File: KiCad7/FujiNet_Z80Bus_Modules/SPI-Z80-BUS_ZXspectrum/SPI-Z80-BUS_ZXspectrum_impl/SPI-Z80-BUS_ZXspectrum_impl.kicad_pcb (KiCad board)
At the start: 2 copper layers, 155 x 55 mm, 29 parts, among them IC1 74HC32N, J1 PinHeader_2.54mm, J2 Z80_CONTROL

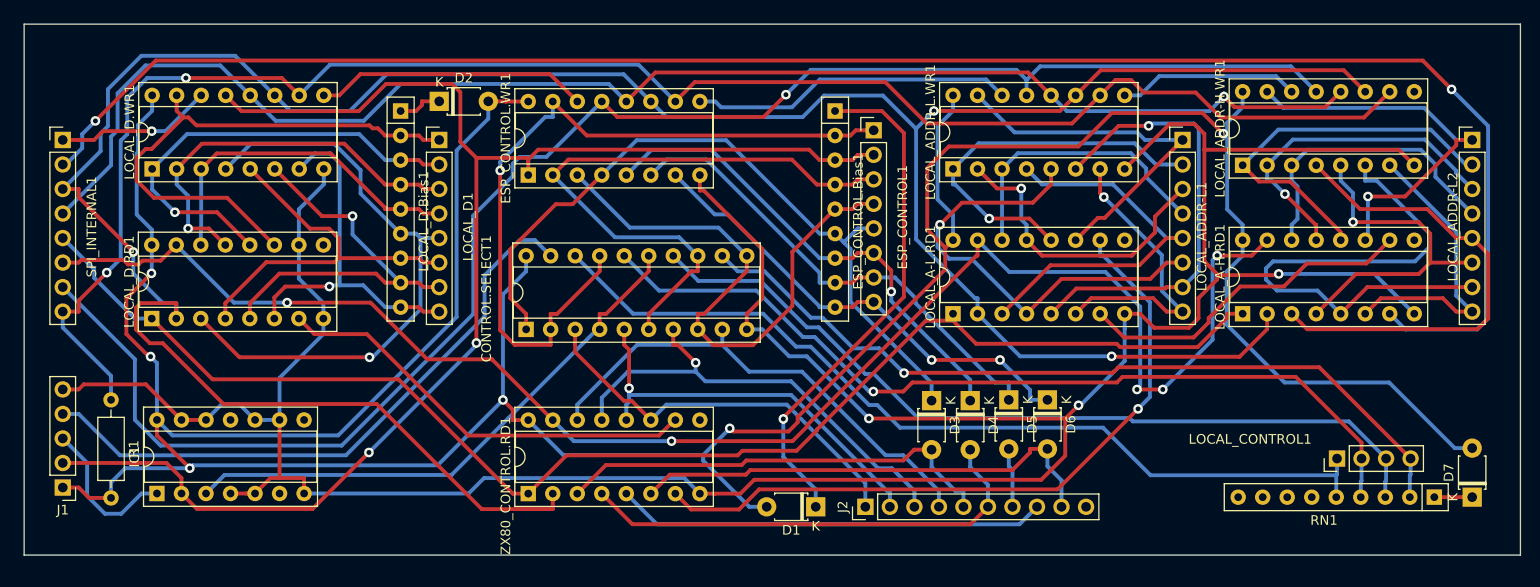
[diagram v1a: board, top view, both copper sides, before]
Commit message: KICad fixed SPI impl
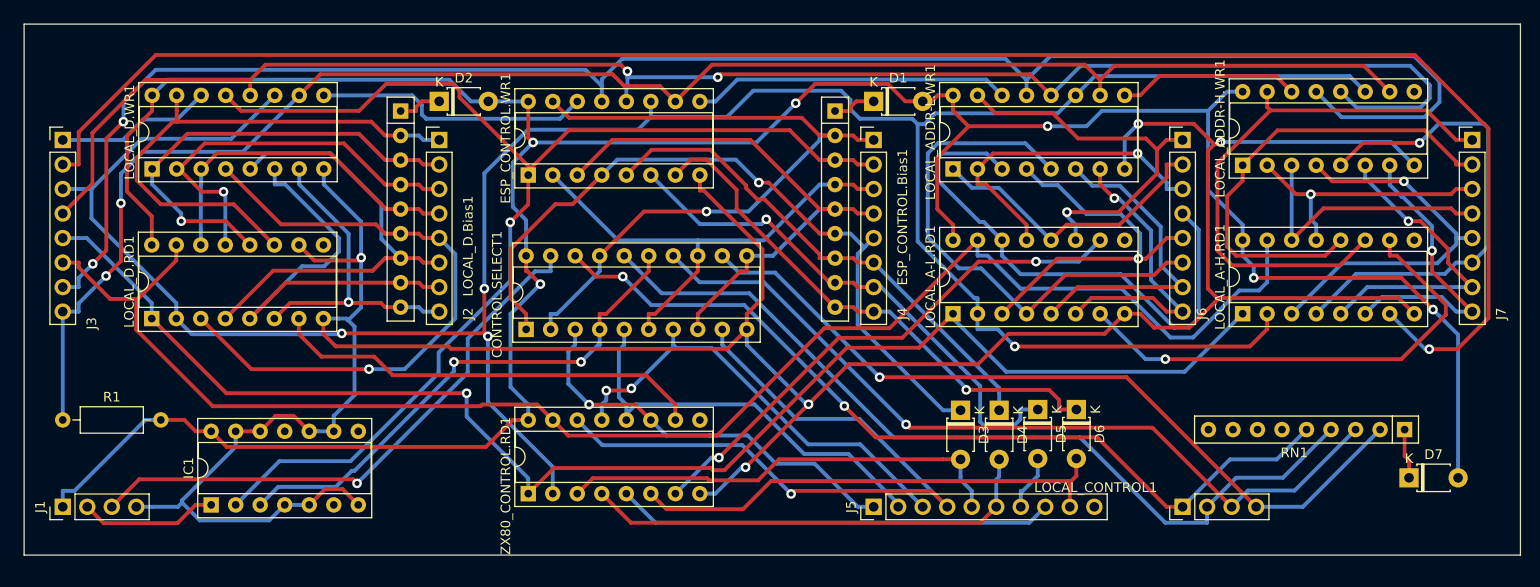
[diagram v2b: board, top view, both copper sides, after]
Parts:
- J1: footprint Connector_PinHeader_2.54mm:PinHeader_1x05_P2.54mm_Vertical -> Connector_PinHeader_2.54mm:PinHeader_1x04_P2.54mm_Vertical
- J2: renamed from LOCAL_D1; value PinHeader_2.54mm -> LOCAL_D
- J3: renamed from SPI_INTERNAL1; value PinHeader_2.54mm -> ESP_SPI_INT
- J4: renamed from ESP_CONTROL1; value PinHeader_2.54mm -> ESP_CONTROL
- J6: renamed from LOCAL_ADDR-L1; value PinHeader_2.54mm -> LOCAL_A-L
- J7: renamed from LOCAL_ADDR-L2; value PinHeader_2.54mm -> LOCAL_A-H
- LOCAL_CONTROL1: value PinHeader_2.54mm -> LOCAL_CONTROL
- moved D1 42.4 mm to (143.0, 35.0), turned to 0 degrees
- moved LOCAL_CONTROL1 16.8 mm to (175.0, 77.0)
- moved RN1 7.65 mm to (198.0, 69.0)
- moved D7 6.84 mm to (198.5, 74.0), turned to 0 degrees
- moved IC1 5.74 mm to (74.4, 76.8)
- moved R1 5.42 mm to (59.0, 68.0), turned to 0 degrees
- moved D3 3.16 mm to (152.0, 67.0)
- moved D4 3.16 mm to (156.0, 67.0)
- moved D5 3.16 mm to (160.0, 66.9)
- moved D6 3.16 mm to (164.0, 66.9)
- moved J1 2.00 mm to (59.0, 77.0), turned to 90 degrees
- moved J4 1.00 mm to (143.0, 39.0)
- moved J5 0.86 mm to (143.0, 77.0)
- renumbered J2 to J5
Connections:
- J1 pad 2: /SPI-Z80-BUS/ESP_CONTROL.WR -> /SPI-Z80-BUS/ESP_PULSE
- J1 pad 3: /SPI-Z80-BUS/ESP_PULSE -> /SPI-Z80-BUS/!ESP_HARDLOCK
- J1 pad 4: /SPI-Z80-BUS/!ESP_HARDLOCK -> GND
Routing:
- net +5V: track 362.0 -> 303.1 mm
- net Net-(D1-K): track 53.4 -> 4.65 mm, vias 1 -> 0
- net /SPI-Z80-BUS/LOCAL_A3: track 29.9 -> 56.1 mm
- net /SPI-Z80-BUS/Z80_CONTROL.MEMRQ: track 51.1 -> 74.2 mm, vias 0 -> 1
- net /SPI-Z80-BUS/ESP_SPI_INT.SCK: track 292.8 -> 270.0 mm, vias 3 -> 4
- net /SPI-Z80-BUS/ESP_CONTROL.WR: track 150.1 -> 127.9 mm, vias 2 -> 1
- net /SPI-Z80-BUS/LOCAL_A14: track 54.9 -> 32.9 mm, vias 0 -> 1
- net /SPI-Z80-BUS/ESP_SPI_INT.STC: track 152.1 -> 170.9 mm, vias 1 -> 2
- net Net-(LOCAL_A-L.RD1-DS): track 73.2 -> 54.9 mm, vias 1 -> 2
- net /SPI-Z80-BUS/ESP_SPI_INT.OE: track 168.2 -> 185.6 mm, vias 1 -> 2
- net /SPI-Z80-BUS/LOCAL_A8: track 41.5 -> 58.1 mm, vias 1 -> 0
- net Net-(LOCAL_A-H.RD1-DS): track 35.5 -> 50.2 mm, vias 0 -> 1
- net /SPI-Z80-BUS/LOCAL_A13: track 36.3 -> 50.2 mm
- net /SPI-Z80-BUS/LOCAL_A6: track 46.8 -> 33.3 mm, vias 1 -> 0
- net /SPI-Z80-BUS/ESP_CONTROL.IORQ: track 63.8 -> 50.3 mm
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
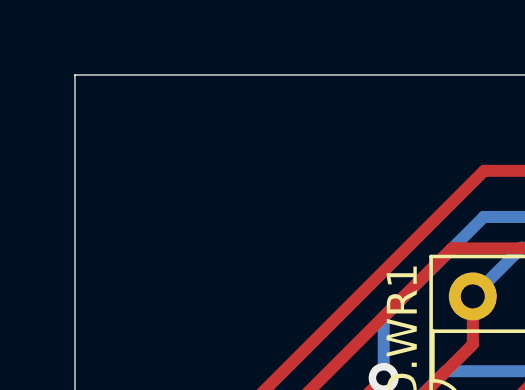
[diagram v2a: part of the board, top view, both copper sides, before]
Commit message: KiCad Corrected the orientation of the impl PCBs
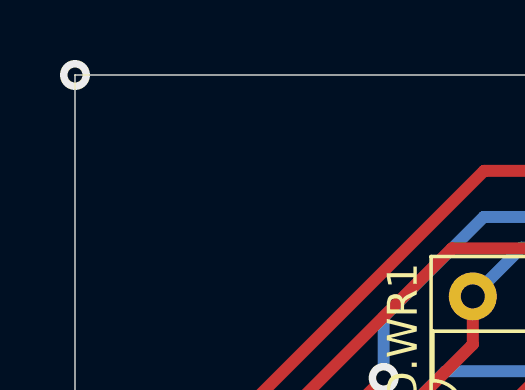
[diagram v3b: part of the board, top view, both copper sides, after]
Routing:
- net (no net): vias 0 -> 1
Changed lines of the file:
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@@
     (style (thickness 0.1) (arrow_length 1.27) (text_position_mode 0) (extension_height 0.58642) (extension_offset 0.5) keep_text_aligned)
   )
+  (via (at 55 27) (size 1) (drill 0.5) (layers "F.Cu" "B.Cu") (net 0))
   (segment (start 138.5079 48.7) (end 139 48.7) (width 0.4) (layer "F.Cu") (net 1))
   (segment (start 132.1147 43.4148) (end 137.3999 48.7) (width 0.4) (layer "F.Cu") (net 1))

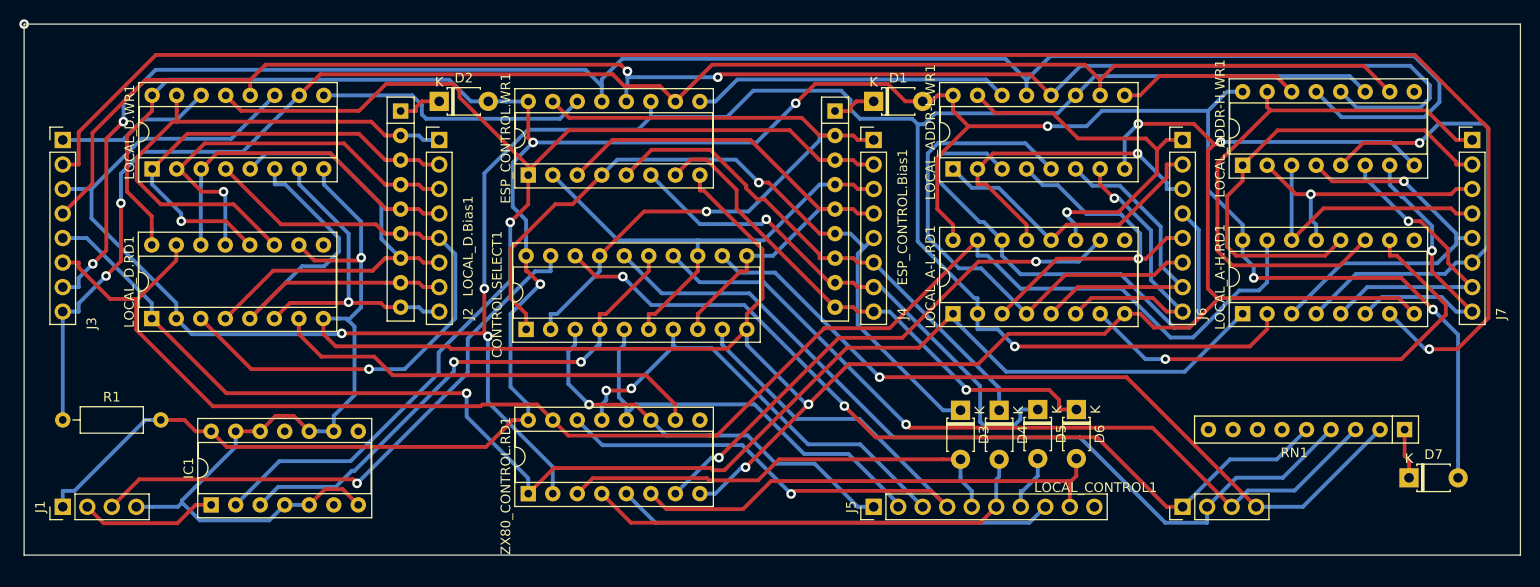
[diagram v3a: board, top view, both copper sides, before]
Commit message: KiCad SPI fixed
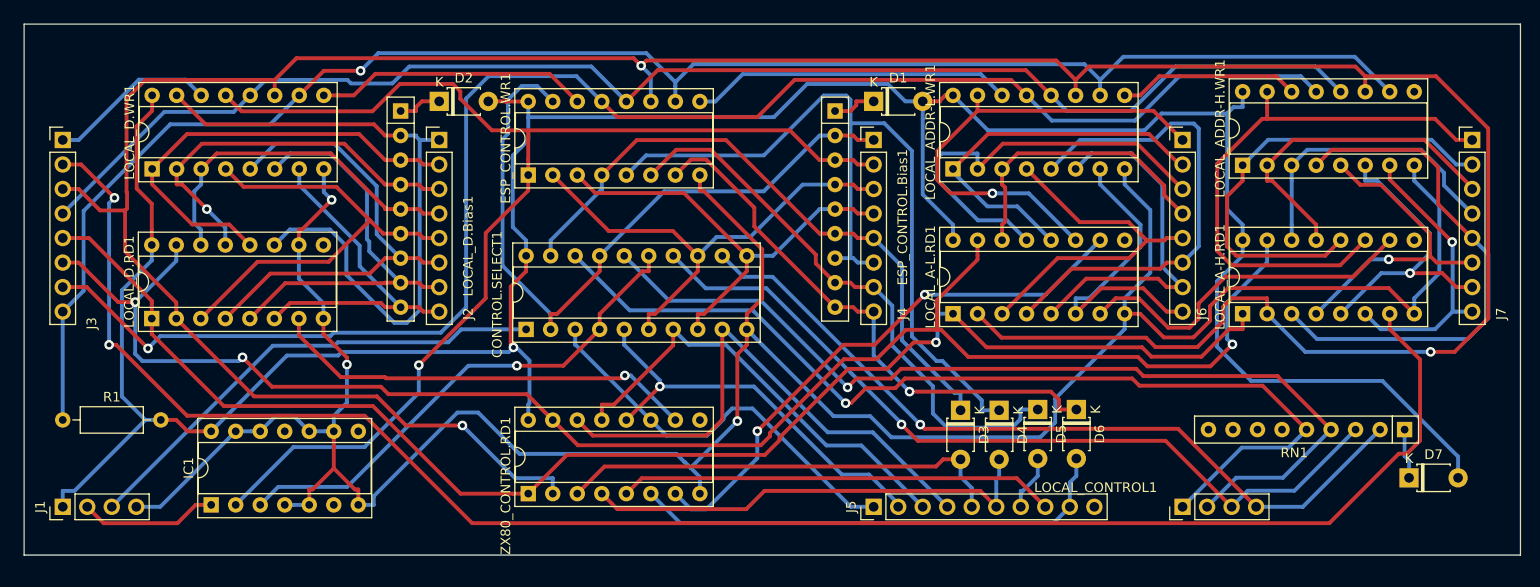
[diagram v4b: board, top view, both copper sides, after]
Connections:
- CONTROL.SELECT1 pad 1: /SPI-Z80-BUS/ESP_CONTROL.BUSRQ -> /SPI-Z80-BUS/!ESP_HARDLOCK
- CONTROL.SELECT1 pad 19: /SPI-Z80-BUS/!ESP_HARDLOCK -> /SPI-Z80-BUS/ESP_CONTROL.BUSRQ
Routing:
- net /SPI-Z80-BUS/ESP_SPI_INT.SCK: track 270.0 -> 317.9 mm, vias 4 -> 3
- net /SPI-Z80-BUS/ESP_CONTROL.WAIT: track 52.6 -> 87.0 mm
- net GND: track 301.4 -> 275.2 mm, vias 5 -> 3
- net /SPI-Z80-BUS/LOCAL_A3: track 56.1 -> 30.2 mm
- net /SPI-Z80-BUS/ESP_SPI_INT.STC: track 170.9 -> 146.6 mm, vias 2 -> 0
- net /SPI-Z80-BUS/ESP_SPI_INT.OE: track 185.6 -> 164.5 mm, vias 2 -> 1
- net /SPI-Z80-BUS/LOCAL_D4: track 64.8 -> 46.8 mm, vias 1 -> 0
- net /SPI-Z80-BUS/Z80_CONTROL.MEMRQ: track 74.2 -> 56.6 mm, vias 1 -> 0
- net /SPI-Z80-BUS/LOCAL_A13: track 50.2 -> 33.4 mm
- net +5V: track 303.1 -> 286.8 mm, vias 6 -> 1
- net /SPI-Z80-BUS/LOCAL_A12: track 40.2 -> 54.2 mm, vias 1 -> 0
- net Net-(LOCAL_A-H.RD1-DS): track 50.2 -> 36.6 mm, vias 1 -> 0
- net /SPI-Z80-BUS/LOCAL_D0: track 55.8 -> 68.8 mm
- net /SPI-Z80-BUS/LOCAL_CONTROL.RD: track 89.9 -> 101.5 mm, vias 2 -> 1
- net /SPI-Z80-BUS/ESP_CONTROL.BUSRQ: track 77.2 -> 66.4 mm, vias 1 -> 0
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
